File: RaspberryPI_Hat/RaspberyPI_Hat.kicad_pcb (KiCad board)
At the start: 2 copper layers, 65 x 56 mm, 46 parts, among them Q1 BC817, Q2 BC817, Q3 BC817, SW1 SW_PUSH, U1 CAT24C32WI-GT3

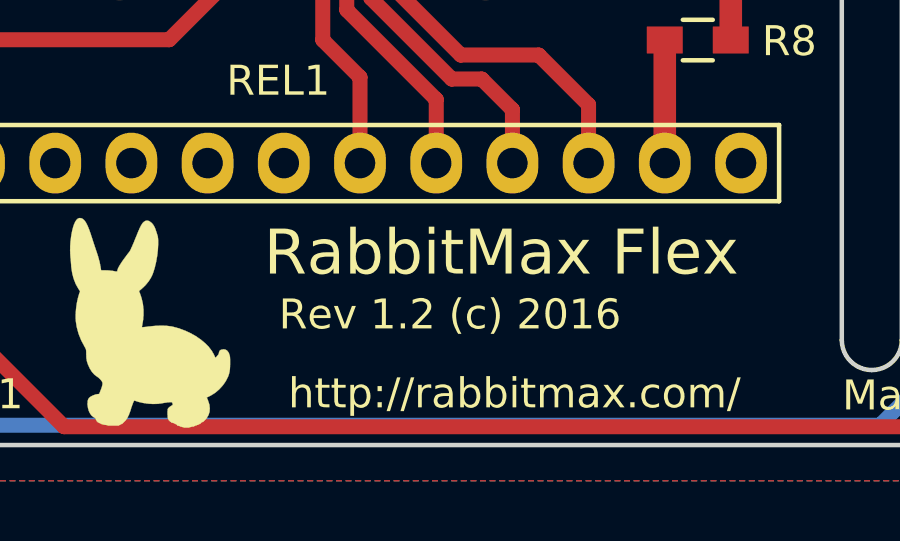
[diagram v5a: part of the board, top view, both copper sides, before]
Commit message: RaspberyPI_Hat.kicad_pcb: Set version to 1.3
Signed-off-by: Leon Anavi <leon@anavi.org>
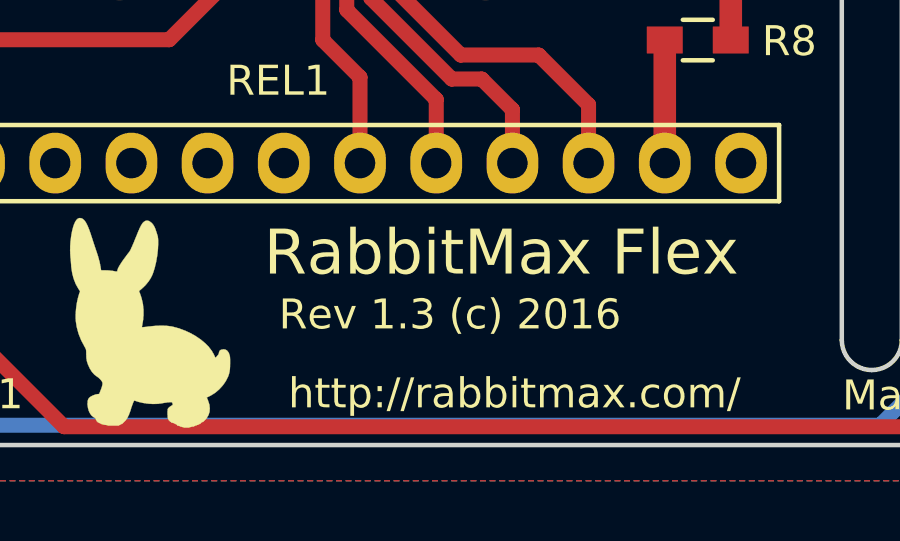
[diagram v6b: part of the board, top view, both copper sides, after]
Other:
- board text added: "Rev 1.3 (c) 2016"
- board text removed: "Rev 1.2 (c) 2016"
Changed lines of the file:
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@@
-(kicad_pcb (version 4) (host pcbnew 4.0.4+e1-6308~48~ubuntu16.04.1-stable)
+(kicad_pcb (version 4) (host pcbnew 4.0.2+dfsg1-stable)
   (general
     (links 112)
     (no_connects 1)
-    (area 97.924999 68.524999 163.075001 124.675001)
+    (area 86.242429 56.842428 174.757572 125.790001)
     (thickness 1.6)
     (drawings 45)
@@
   )
   (setup
-    (last_trace_width 0.754)
+    (last_trace_width 0.5)
     (user_trace_width 0.254)
     (user_trace_width 0.5)
@@
     (effects (font (size 1 1) (thickness 0.25)))
   )
-  (gr_text "Rev 1.2 (c) 2016" (at 128.94 120.25) (layer F.SilkS)
+  (gr_text "Rev 1.3 (c) 2016" (at 128.94 120.25) (layer F.SilkS)
     (effects (font (size 1 1) (thickness 0.25)))
   )
